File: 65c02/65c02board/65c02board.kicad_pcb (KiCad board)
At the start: 2 copper layers, 6 parts, among them J1 Conn_01x34_Male, U1 W65C02, U2 74HC00

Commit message: Reworked schematics for the WD65C02 processor board.
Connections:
- C1 pad 1: /GND -> /5V
- C2 pad 2: /GND -> /5V
- J1 pad 1: /GND -> /5V
- J1 pad 10: /GND -> /5V
- J1 pad 8: /GND -> /5V
- J1 pad 9: /GND -> /5V
- U1 pad 21: /GND -> /5V
- U2 pad 7: /GND -> /5V
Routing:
- added copper zone on B.Cu, net /5V
- removed copper zone on B.Cu, net /GND
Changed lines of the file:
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@@
     (zones 0)
     (modules 6)
-    (nets 41)
+    (nets 40)
   )
   (page A4)
@@
   )
   (setup
-    (last_trace_width 0.4)
+    (last_trace_width 0.25)
     (user_trace_width 0.4)
     (user_trace_width 1)
@@
     (pad_to_mask_clearance 0.2)
     (aux_axis_origin 0 0)
-    (visible_elements FFFFFF7F)
+    (visible_elements 7FFFFFFF)
     (pcbplotparams
       (layerselection 0x010fc_ffffffff)
@@
   (net 38 "Net-(U1-Pad39)")
   (net 39 "Net-(U2-Pad11)")
-  (net 40 /GND)
   (net_class Default "Dies ist die voreingestellte Netzklasse."
     (clearance 0.2)
@@
     (add_net /D6)
     (add_net /D7)
-    (add_net /GND)
     (add_net /RD)
     (add_net /RES)
@@
       (net 36 "Net-(U1-Pad34)"))
     (pad 7 thru_hole oval (at 0 15.24) (size 1.6 1.6) (drill 0.8) (layers *.Cu *.Mask)
-      (net 40 /GND))
+      (net 1 /5V))
     (pad 14 thru_hole oval (at 7.62 0) (size 1.6 1.6) (drill 0.8) (layers *.Cu *.Mask)
       (net 1 /5V))
@@
       (net 31 "Net-(U1-Pad1)"))
     (pad 21 thru_hole oval (at 15.24 48.26 180) (size 1.6 1.6) (drill 0.8) (layers *.Cu *.Mask)
-      (net 40 /GND))
+      (net 1 /5V))
     (pad 2 thru_hole oval (at 0 2.54 180) (size 1.6 1.6) (drill 0.8) (layers *.Cu *.Mask)
       (net 30 "Net-(R1-Pad1)"))
@@
     )
     (pad 1 thru_hole circle (at 0 0) (size 1.6 1.6) (drill 0.8) (layers *.Cu *.Mask)
-      (net 40 /GND))
+      (net 1 /5V))
     (pad 2 thru_hole circle (at 2.5 0) (size 1.6 1.6) (drill 0.8) (layers *.Cu *.Mask)
       (net 1 /5V))
@@
     (fp_line (start -0.25 -1) (end -0.25 1) (layer F.Fab) (width 0.1))
     (pad 2 thru_hole circle (at 2.5 0 90) (size 1.6 1.6) (drill 0.8) (layers *.Cu *.Mask)
-      (net 40 /GND))
+      (net 1 /5V))
     (pad 1 thru_hole circle (at 0 0 90) (size 1.6 1.6) (drill 0.8) (layers *.Cu *.Mask)
       (net 1 /5V))
@@
     )
     (pad 1 thru_hole rect (at 0 0 180) (size 1.7 1.7) (drill 1) (layers *.Cu *.Mask)
-      (net 40 /GND))
+      (net 1 /5V))
     (pad 2 thru_hole oval (at 0 -2.54 180) (size 1.7 1.7) (drill 1) (layers *.Cu *.Mask)
       (net 1 /5V))
@@
       (net 6 /A19))
     (pad 8 thru_hole oval (at 0 -17.78 180) (size 1.7 1.7) (drill 1) (layers *.Cu *.Mask)
-      (net 40 /GND))
+      (net 1 /5V))
     (pad 9 thru_hole oval (at 0 -20.32 180) (size 1.7 1.7) (drill 1) (layers *.Cu *.Mask)
-      (net 40 /GND))
+      (net 1 /5V))
     (pad 10 thru_hole oval (at 0 -22.86 180) (size 1.7 1.7) (drill 1) (layers *.Cu *.Mask)
-      (net 40 /GND))
+      (net 1 /5V))
     (pad 11 thru_hole oval (at 0 -25.4 180) (size 1.7 1.7) (drill 1) (layers *.Cu *.Mask)
       (net 1 /5V))
@@
   (segment (start 142.24 63.5) (end 144.78 63.5) (width 0.4) (layer F.Cu) (net 39))
   (segment (start 139.7 66.04) (end 142.24 63.5) (width 0.4) (layer F.Cu) (net 39))
-  (zone (net 40) (net_name /GND) (layer B.Cu) (hatch edge 0.508)
+  (zone (net 1) (net_name /5V) (layer B.Cu) (hatch edge 0.508)
     (connect_pads (clearance 0.2))
     (min_thickness 0.254)

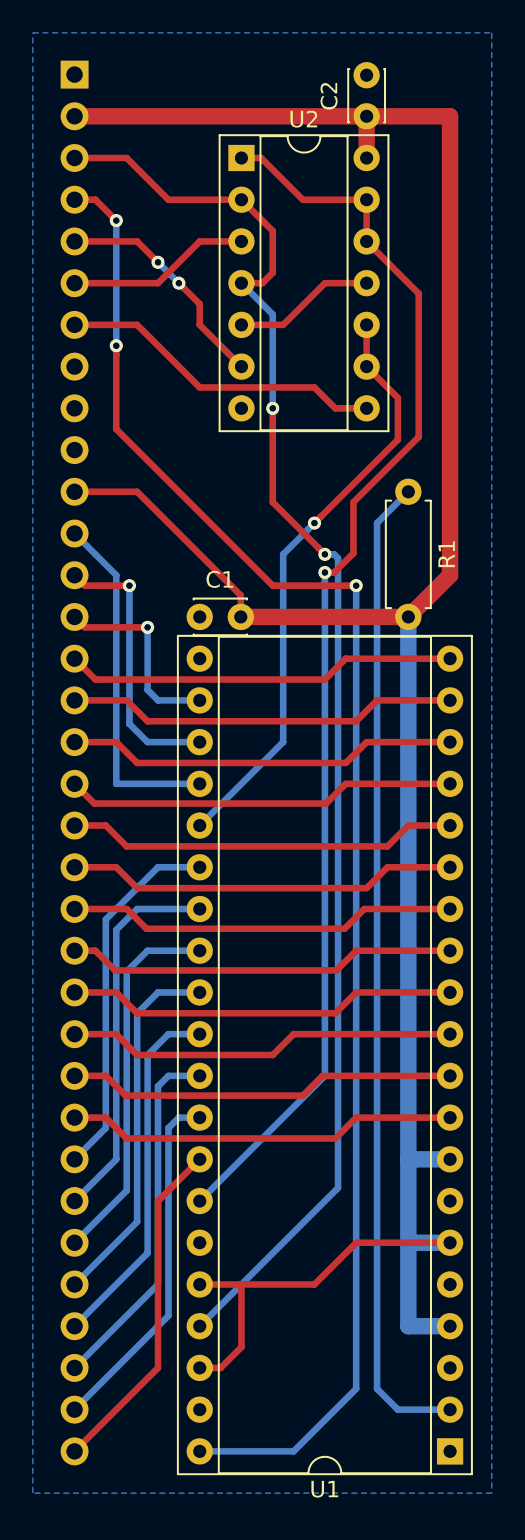
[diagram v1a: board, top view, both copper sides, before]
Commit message: Tweak schematics to only use one GND and one +5V rail
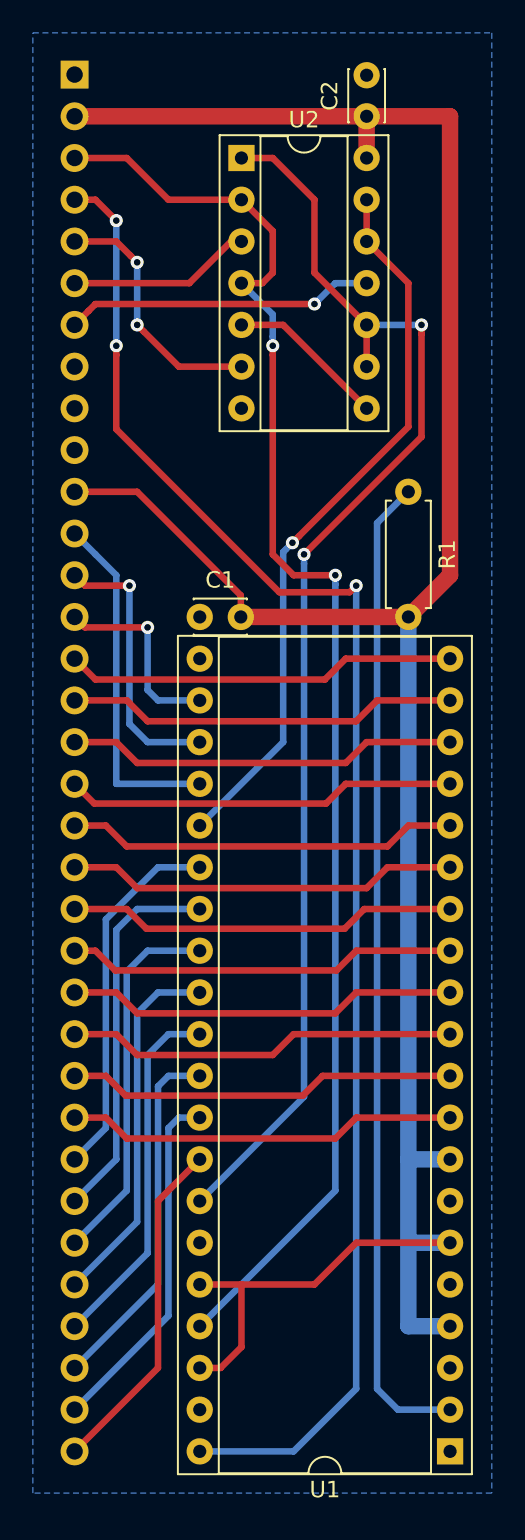
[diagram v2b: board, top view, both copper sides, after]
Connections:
- C1 pad 1: /5V -> /GND
- C2 pad 2: /5V -> /GND
- J1 pad 1: /5V -> /GND
- J1 pad 10: /5V -> /GND
- J1 pad 7: /A19 -> /RAM
- J1 pad 8: /5V -> /GND
- J1 pad 9: /5V -> /GND
- U1 pad 21: /5V -> /GND
- U2 pad 10: Net-(U1-Pad25) -> Net-(U1-Pad34)
- U2 pad 11: Net-(U2-Pad11) -> /RAM
- U2 pad 12: Net-(U1-Pad34) -> Net-(U1-Pad25)
- U2 pad 13: Net-(U1-Pad34) -> Net-(U1-Pad25)
- U2 pad 5: Net-(U2-Pad11) -> Net-(U2-Pad5)
- U2 pad 7: /5V -> /GND
- U2 pad 8: /A19 -> Net-(U2-Pad5)
- U2 pad 9: Net-(U1-Pad25) -> Net-(U1-Pad34)
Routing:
- net /A19: track 19.9 -> 0.00 mm
- net /RAM: track 0.00 -> 18.8 mm, vias 0 -> 1
- net Net-(U2-Pad5): track 0.00 -> 9.72 mm
- net Net-(U2-Pad11): track 8.67 -> 0.00 mm
- net Net-(U1-Pad25): track 36.3 -> 44.4 mm
- net Net-(U1-Pad34): track 76.8 -> 79.2 mm, vias 1 -> 2
- net /WR: track 14.1 -> 15.5 mm
- net /CLK: track 88.4 -> 89.4 mm
- added copper zone on B.Cu, net /GND
- removed copper zone on B.Cu, net /5V

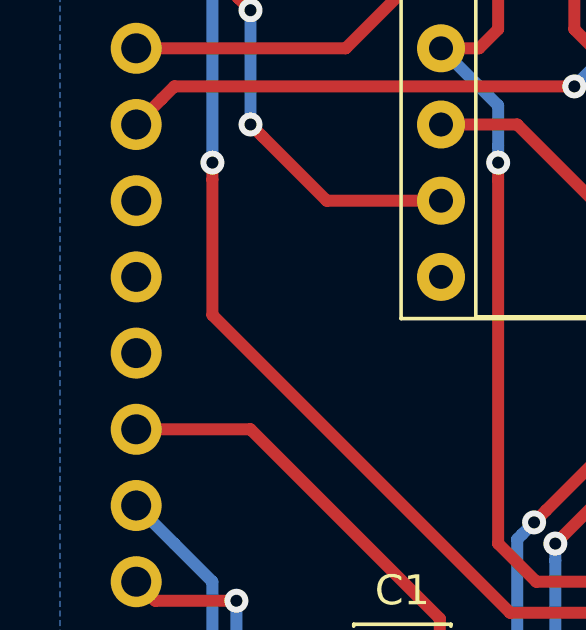
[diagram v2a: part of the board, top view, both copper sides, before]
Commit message: Rework schematics and documentation
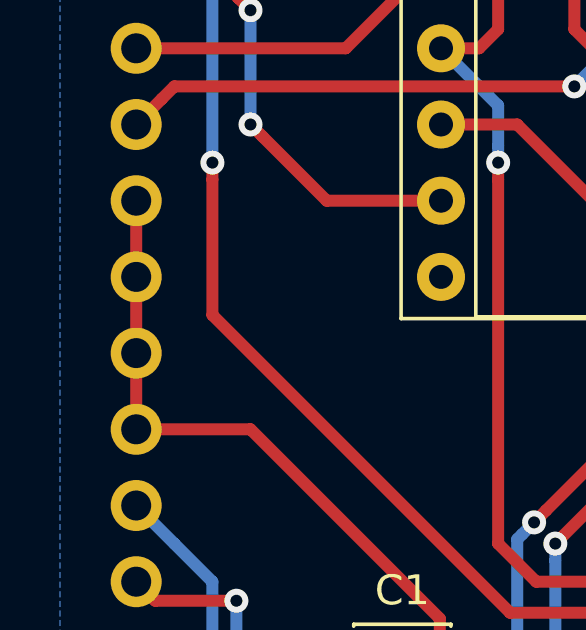
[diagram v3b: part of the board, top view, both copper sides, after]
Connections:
- J1 pad 10: /GND -> /5V
- J1 pad 8: /GND -> /5V
- J1 pad 9: /GND -> /5V
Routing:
- net /5V: track 155.1 -> 162.8 mm
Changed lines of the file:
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@@
     (thickness 1.6)
     (drawings 0)
-    (tracks 208)
+    (tracks 211)
     (zones 0)
     (modules 6)
@@
       (net 39 /RAM))
     (pad 8 thru_hole oval (at 0 -17.78 180) (size 1.7 1.7) (drill 1) (layers *.Cu *.Mask)
-      (net 38 /GND))
+      (net 1 /5V))
     (pad 9 thru_hole oval (at 0 -20.32 180) (size 1.7 1.7) (drill 1) (layers *.Cu *.Mask)
-      (net 38 /GND))
+      (net 1 /5V))
     (pad 10 thru_hole oval (at 0 -22.86 180) (size 1.7 1.7) (drill 1) (layers *.Cu *.Mask)
-      (net 38 /GND))
+      (net 1 /5V))
     (pad 11 thru_hole oval (at 0 -25.4 180) (size 1.7 1.7) (drill 1) (layers *.Cu *.Mask)
       (net 1 /5V))
@@
   (segment (start 137.16 124.46) (end 137.16 128.27) (width 0.4) (layer F.Cu) (net 1))
   (segment (start 137.16 128.27) (end 135.89 129.54) (width 0.4) (layer F.Cu) (net 1))
+  (segment (start 127 76.2) (end 127 73.66) (width 0.4) (layer F.Cu) (net 1))
+  (segment (start 127 73.66) (end 127 71.12) (width 0.4) (layer F.Cu) (net 1))
+  (segment (start 127 71.12) (end 127 68.58) (width 0.4) (layer F.Cu) (net 1))
   (segment (start 127 55.88) (end 130.175 55.88) (width 0.4) (layer F.Cu) (net 2))
   (segment (start 132.715 58.42) (end 137.16 58.42) (width 0.4) (layer F.Cu) (net 2))

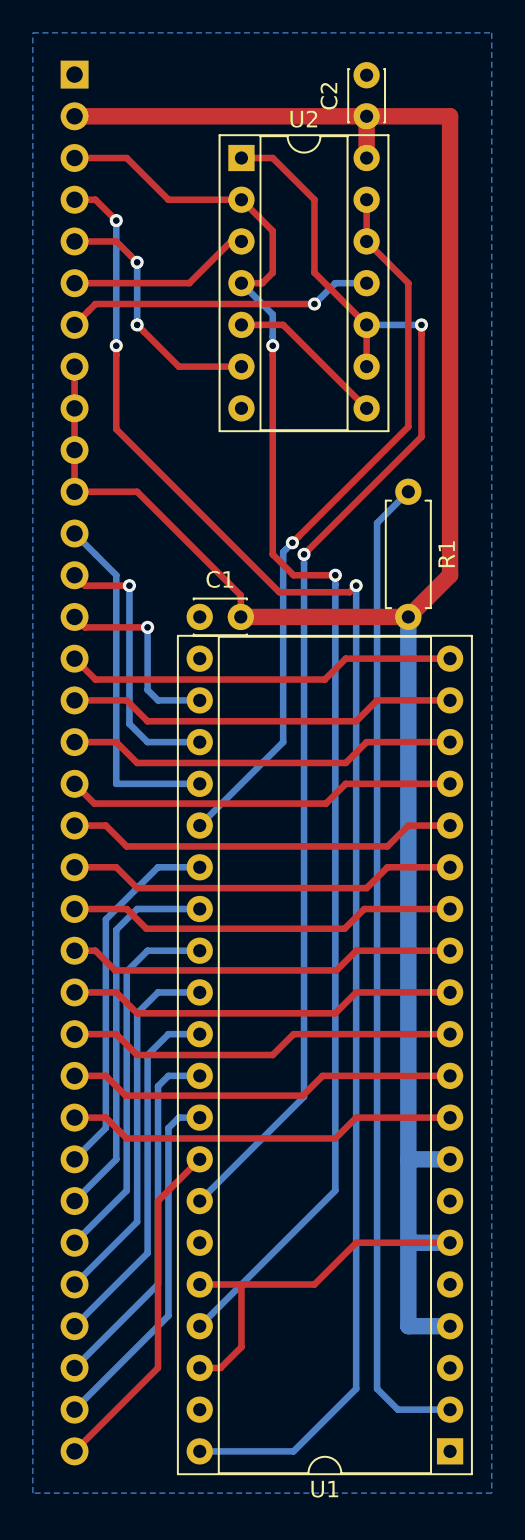
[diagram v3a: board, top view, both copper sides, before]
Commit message: Remove unnecessary pullup at Rdy pin
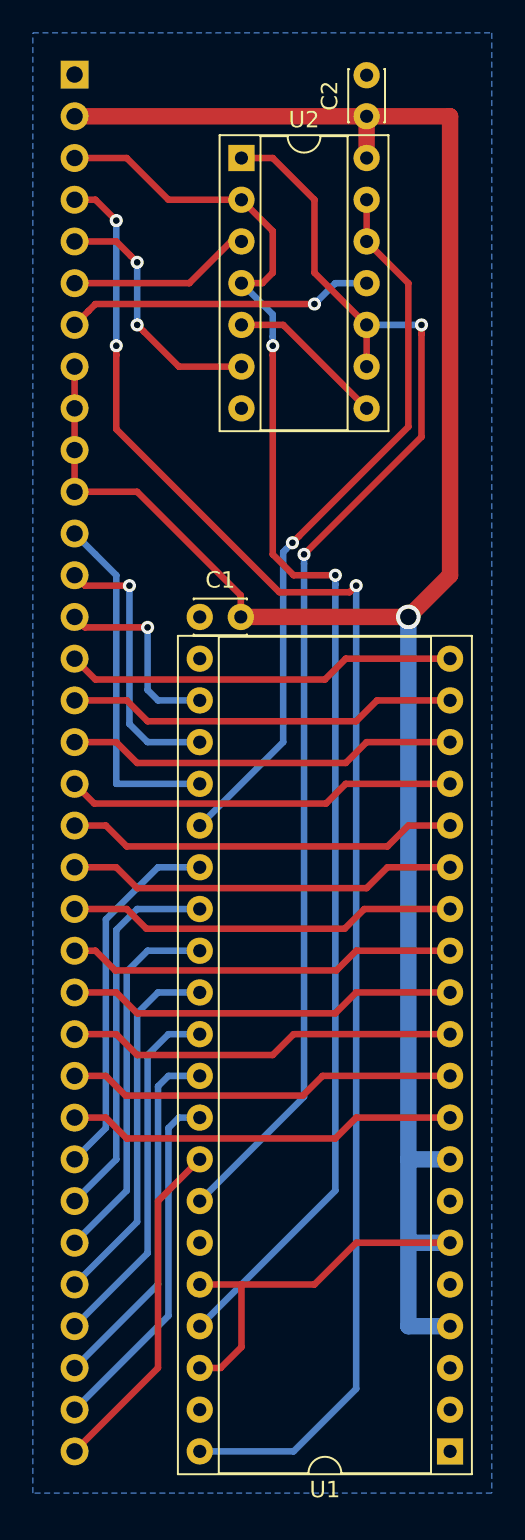
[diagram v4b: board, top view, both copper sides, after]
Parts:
- removed R1: 1k, Resistor_THT:R_Axial_DIN0207_L6.3mm_D2.5mm_P7.62mm_Horizontal
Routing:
- net Net-(U1-Pad2): track 60.4 -> 0.00 mm
- net /5V: vias 0 -> 1

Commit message: Switch meaning of the A19 pin from RAM to ROM. Use pull-ups instead of pull-downs for the input port.
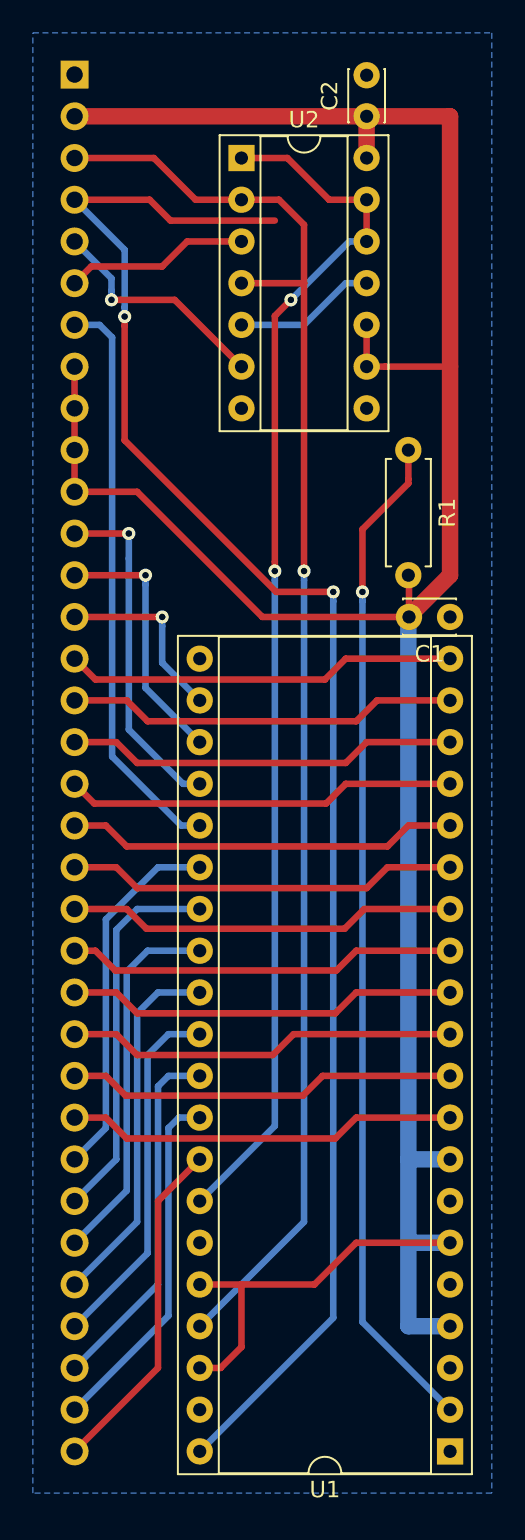
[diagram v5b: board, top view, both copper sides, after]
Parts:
- added R1: 1k, Resistor_THT:R_Axial_DIN0207_L6.3mm_D2.5mm_P7.62mm_Horizontal, F.Cu at (147.3, 73.7)
- moved C1 15.2 mm to (149.9, 83.8), turned to 180 degrees
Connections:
- net /RD renamed /RD#
- net /RES renamed /RES#
- net /WR renamed /WR#
- J1 pad 7: /RAM -> /ROM
- U1 pad 25: Net-(U1-Pad25) -> /ROM
- U2 pad 10: Net-(U1-Pad34) -> /5V
- U2 pad 11: /RAM -> Net-(U2-Pad11)
- U2 pad 12: Net-(U1-Pad25) -> Net-(U1-Pad34)
- U2 pad 13: Net-(U1-Pad25) -> Net-(U1-Pad34)
- U2 pad 5: Net-(U2-Pad5) -> Net-(U2-Pad11)
- U2 pad 8: Net-(U2-Pad5) -> Net-(U2-Pad8)
- U2 pad 9: Net-(U1-Pad34) -> /5V
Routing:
- net Net-(R1-Pad1): track 0.00 -> 61.8 mm, vias 0 -> 1
- net Net-(U1-Pad25): track 44.4 -> 0.00 mm, vias 1 -> 0
- net /ROM: track 0.00 -> 35.2 mm
- net /RAM: track 18.8 -> 0.00 mm, vias 1 -> 0
- net Net-(U2-Pad5): track 9.72 -> 0.00 mm
- net /5V: track 162.8 -> 172.2 mm, vias 1 -> 0
- net Net-(U2-Pad11): track 0.00 -> 8.67 mm
- net /RES#: track 94.6 -> 100.8 mm, vias 3 -> 2
- net Net-(U1-Pad34): track 79.2 -> 74.5 mm
- net /WR#: track 15.5 -> 14.1 mm, vias 2 -> 1
- net /A13: track 16.8 -> 15.8 mm
- net /A12: track 12.0 -> 11.4 mm
- net /A14: track 21.4 -> 20.9 mm, vias 0 -> 1
- net /CLK: track 89.4 -> 89.1 mm, vias 2 -> 1
